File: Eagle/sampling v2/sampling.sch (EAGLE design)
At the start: 8 parts, among them X1 JST-XH-04-PIN-LONG-PAD

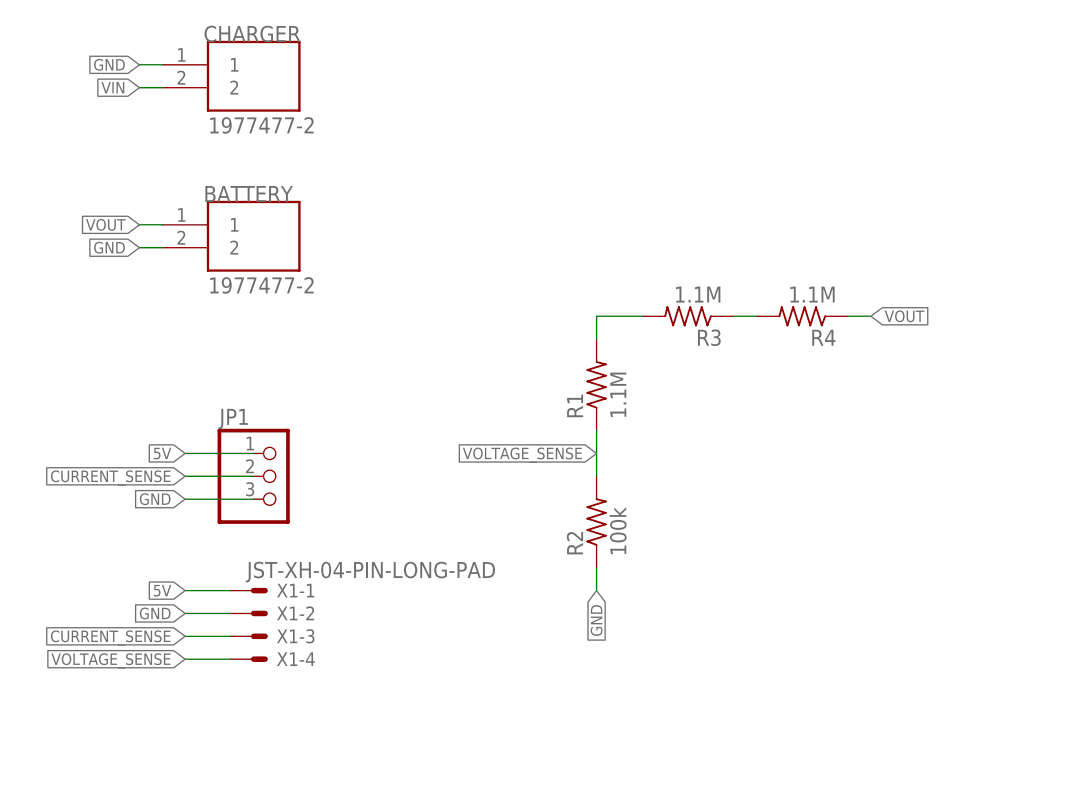
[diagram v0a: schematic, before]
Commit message: update sampling board
zener, divider HV, update divider batt
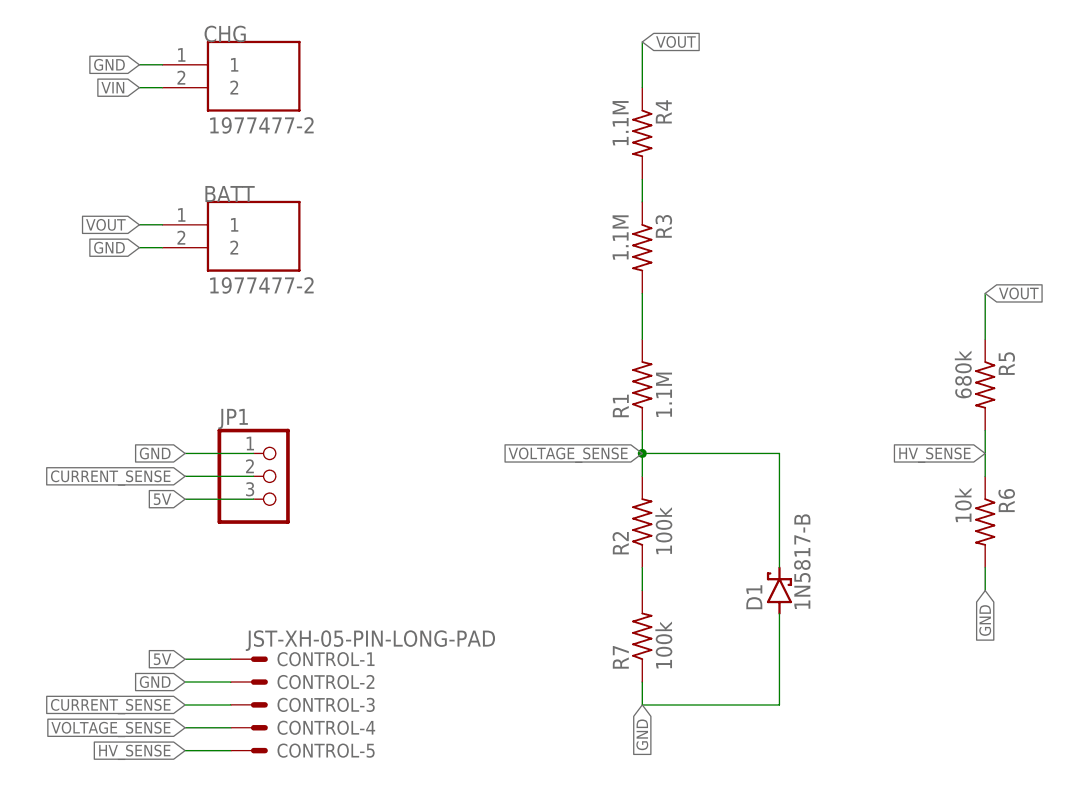
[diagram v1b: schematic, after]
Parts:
- removed X1: JST-XH-04-PIN-LONG-PAD, Rembrandt Electronics - JST XH Connectors v1-0:JST-XH-04-PIN-LONG-PAD
- added CONTROL: JST-XH-05-PIN-LONG-PAD, Rembrandt Electronics - JST XH Connectors v1-0:JST-XH-05-PIN-LONG-PAD
- added D1: 1N5817-B, diode:1N5817-B
- added R5: 680k, rcl:R-US_0207/10
- added R6: 10k, rcl:R-US_0207/10
- added R7: 100k, rcl:R-US_R0805
- renumbered BATTERY to BATT, CHARGER to CHG
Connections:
- new net HV_SENSE: CONTROL-5.S, R5.2, R6.1
- new net N$3: R2.1, R7.2
- net 5V: now also CONTROL-1.S, JP1.3; no longer JP1.1, X1-1.S
- net CURRENT_SENSE: now also CONTROL-3.S; no longer X1-3.S
- net GND: now also CONTROL-2.S, D1.A, JP1.1, R6.2, R7.1; no longer JP1.3, R2.1, X1-2.S
- net VOLTAGE_SENSE: now also CONTROL-4.S, D1.C; no longer X1-4.S
- net VOUT: now also R5.1
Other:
- moved on the sheet: R1, R2, R3, R4
